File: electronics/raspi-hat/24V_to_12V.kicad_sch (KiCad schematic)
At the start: 11 parts

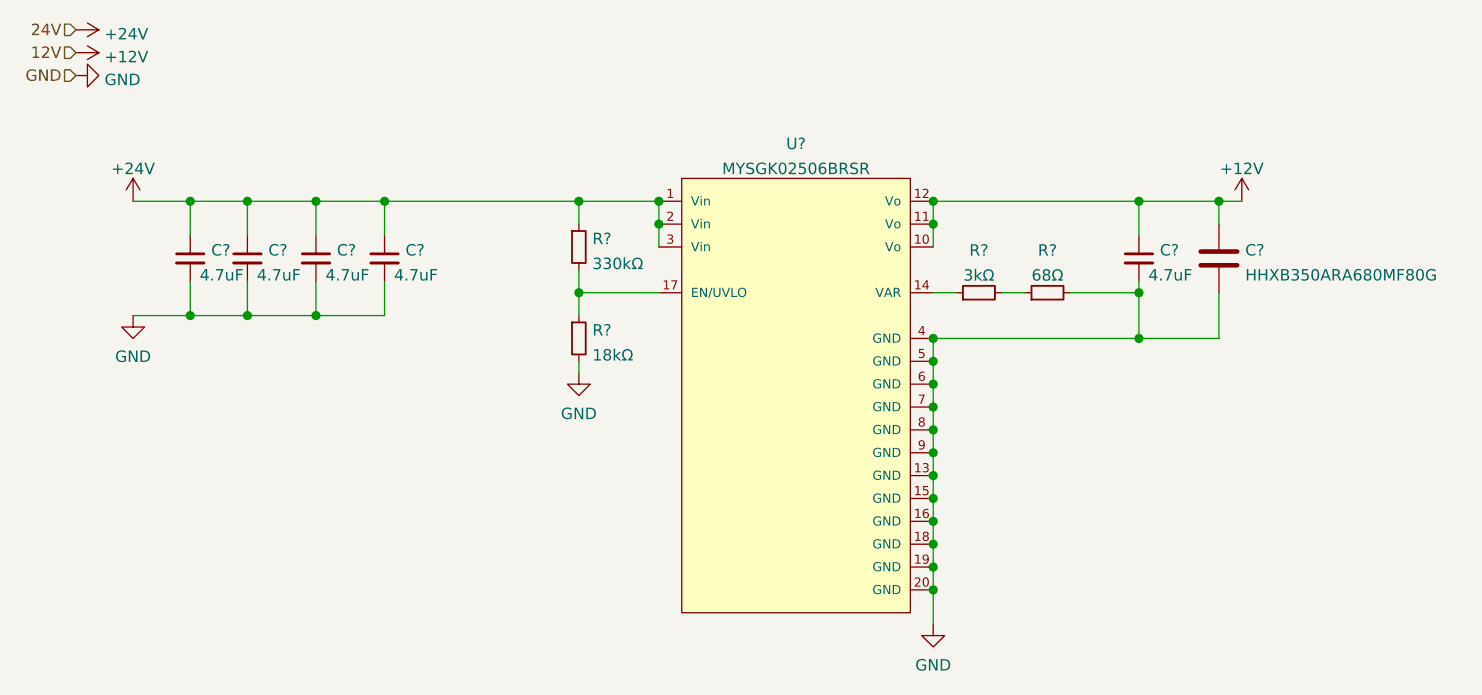
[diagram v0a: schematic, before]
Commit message: Finish adding MYMGA5R04RELA5RA
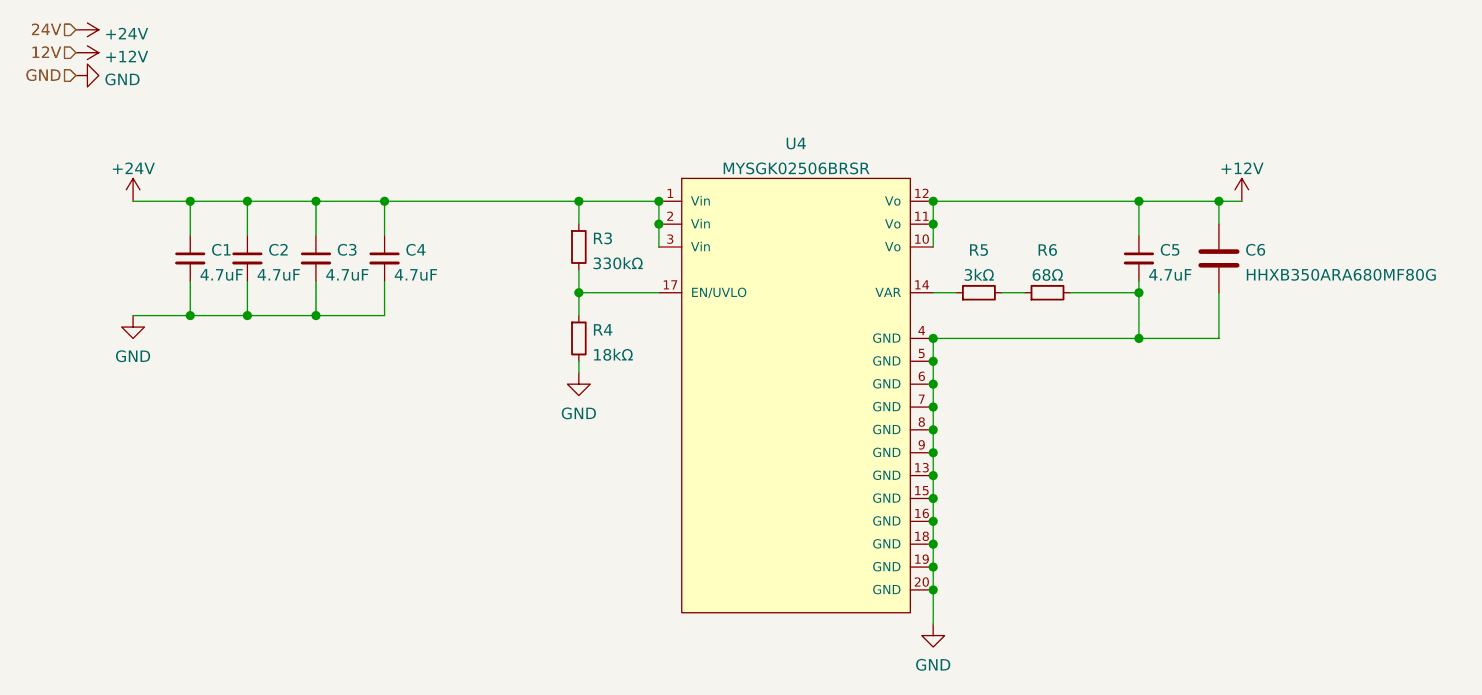
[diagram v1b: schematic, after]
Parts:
- gave numbers to parts that had none: 11
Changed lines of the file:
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@@
   (symbol (lib_id "power:+24V") (at 22.86 20.32 270) (unit 1)
     (in_bom yes) (on_board yes) (fields_autoplaced)
-    (property "Reference" "#PWR?" (id 0) (at 19.05 20.32 0)
+    (property "Reference" "#PWR0111" (id 0) (at 19.05 20.32 0)
       (effects (font (size 1.27 1.27)) hide)
     )
@@
   (symbol (lib_id "power:+12V") (at 22.86 22.86 270) (unit 1)
     (in_bom yes) (on_board yes) (fields_autoplaced)
-    (property "Reference" "#PWR?" (id 0) (at 19.05 22.86 0)
+    (property "Reference" "#PWR0112" (id 0) (at 19.05 22.86 0)
       (effects (font (size 1.27 1.27)) hide)
     )
@@
   (symbol (lib_id "power:+24V") (at 29.21 39.37 0) (unit 1)
     (in_bom yes) (on_board yes) (fields_autoplaced)
-    (property "Reference" "#PWR?" (id 0) (at 29.21 43.18 0)
+    (property "Reference" "#PWR0110" (id 0) (at 29.21 43.18 0)
       (effects (font (size 1.27 1.27)) hide)
     )
@@
   (symbol (lib_id "power:+12V") (at 152.4 39.37 0) (unit 1)
     (in_bom yes) (on_board yes) (fields_autoplaced)
-    (property "Reference" "#PWR?" (id 0) (at 152.4 43.18 0)
+    (property "Reference" "#PWR0108" (id 0) (at 152.4 43.18 0)
       (effects (font (size 1.27 1.27)) hide)
     )
@@
   (symbol (lib_id "power:GND") (at 22.86 25.4 90) (unit 1)
     (in_bom yes) (on_board yes) (fields_autoplaced)
-    (property "Reference" "#PWR?" (id 0) (at 29.21 25.4 0)
+    (property "Reference" "#PWR0113" (id 0) (at 29.21 25.4 0)
       (effects (font (size 1.27 1.27)) hide)
     )
@@
   (symbol (lib_id "power:GND") (at 29.21 52.07 0) (unit 1)
     (in_bom yes) (on_board yes) (fields_autoplaced)
-    (property "Reference" "#PWR?" (id 0) (at 29.21 58.42 0)
+    (property "Reference" "#PWR0109" (id 0) (at 29.21 58.42 0)
       (effects (font (size 1.27 1.27)) hide)
     )
@@
   (symbol (lib_id "power:GND") (at 78.74 58.42 0) (unit 1)
     (in_bom yes) (on_board yes) (fields_autoplaced)
-    (property "Reference" "#PWR?" (id 0) (at 78.74 64.77 0)
+    (property "Reference" "#PWR0114" (id 0) (at 78.74 64.77 0)
       (effects (font (size 1.27 1.27)) hide)
     )
@@
   (symbol (lib_id "power:GND") (at 118.11 86.36 0) (unit 1)
     (in_bom yes) (on_board yes) (fields_autoplaced)
-    (property "Reference" "#PWR?" (id 0) (at 118.11 92.71 0)
+    (property "Reference" "#PWR0107" (id 0) (at 118.11 92.71 0)
       (effects (font (size 1.27 1.27)) hide)
     )
@@
   (symbol (lib_id "Device:R_Small") (at 78.74 44.45 0) (unit 1)
     (in_bom yes) (on_board yes) (fields_autoplaced)
-    (property "Reference" "R?" (id 0) (at 80.2387 43.5415 0)
+    (property "Reference" "R3" (id 0) (at 80.2387 43.5415 0)
       (effects (font (size 1.27 1.27)) (justify left))
     )
@@
   (symbol (lib_id "Device:R_Small") (at 78.74 54.61 0) (unit 1)
     (in_bom yes) (on_board yes) (fields_autoplaced)
-    (property "Reference" "R?" (id 0) (at 80.2387 53.7015 0)
+    (property "Reference" "R4" (id 0) (at 80.2387 53.7015 0)
       (effects (font (size 1.27 1.27)) (justify left))
     )
@@
   (symbol (lib_id "Device:R_Small") (at 123.19 49.53 90) (unit 1)
     (in_bom yes) (on_board yes) (fields_autoplaced)
-    (property "Reference" "R?" (id 0) (at 123.19 44.8268 90))
+    (property "Reference" "R5" (id 0) (at 123.19 44.8268 90))
     (property "Value" "3kΩ" (id 1) (at 123.19 47.6019 90))
     (property "Footprint" "" (id 2) (at 123.19 49.53 0)
@@
   (symbol (lib_id "Device:R_Small") (at 130.81 49.53 90) (unit 1)
     (in_bom yes) (on_board yes) (fields_autoplaced)
-    (property "Reference" "R?" (id 0) (at 130.81 44.8268 90))
+    (property "Reference" "R6" (id 0) (at 130.81 44.8268 90))
     (property "Value" "68Ω" (id 1) (at 130.81 47.6019 90))
     (property "Footprint" "" (id 2) (at 130.81 49.53 0)
@@
   (symbol (lib_id "Device:C_Small") (at 35.56 45.72 0) (unit 1)
     (in_bom yes) (on_board yes)
-    (property "Reference" "C?" (id 0) (at 37.8842 44.8115 0)
+    (property "Reference" "C1" (id 0) (at 37.8842 44.8115 0)
       (effects (font (size 1.27 1.27)) (justify left))
     )
@@
   (symbol (lib_id "Device:C_Small") (at 41.91 45.72 0) (unit 1)
     (in_bom yes) (on_board yes)
-    (property "Reference" "C?" (id 0) (at 44.2342 44.8115 0)
+    (property "Reference" "C2" (id 0) (at 44.2342 44.8115 0)
       (effects (font (size 1.27 1.27)) (justify left))
     )
@@
   (symbol (lib_id "Device:C_Small") (at 49.53 45.72 0) (unit 1)
     (in_bom yes) (on_board yes)
-    (property "Reference" "C?" (id 0) (at 51.8542 44.8115 0)
+    (property "Reference" "C3" (id 0) (at 51.8542 44.8115 0)
       (effects (font (size 1.27 1.27)) (justify left))
     )
@@
   (symbol (lib_id "Device:C_Small") (at 57.15 45.72 0) (unit 1)
     (in_bom yes) (on_board yes)
-    (property "Reference" "C?" (id 0) (at 59.4742 44.8115 0)
+    (property "Reference" "C4" (id 0) (at 59.4742 44.8115 0)
       (effects (font (size 1.27 1.27)) (justify left))
     )
@@
   (symbol (lib_id "Device:C_Small") (at 140.97 45.72 0) (unit 1)
     (in_bom yes) (on_board yes)
-    (property "Reference" "C?" (id 0) (at 143.2942 44.8115 0)
+    (property "Reference" "C5" (id 0) (at 143.2942 44.8115 0)
       (effects (font (size 1.27 1.27)) (justify left))
     )
@@
   (symbol (lib_id "Device:C") (at 149.86 45.72 0) (unit 1)
     (in_bom yes) (on_board yes) (fields_autoplaced)
-    (property "Reference" "C?" (id 0) (at 152.7811 44.8115 0)
+    (property "Reference" "C6" (id 0) (at 152.7811 44.8115 0)
       (effects (font (size 1.27 1.27)) (justify left))
     )
@@
   (symbol (lib_id "MYSGK02506BRSR:MYSGK02506BRSR") (at 85.09 39.37 0) (unit 1)
     (in_bom yes) (on_board yes) (fields_autoplaced)
-    (property "Reference" "U?" (id 0) (at 102.87 32.9904 0))
+    (property "Reference" "U4" (id 0) (at 102.87 32.9904 0))
     (property "Value" "MYSGK02506BRSR" (id 1) (at 102.87 35.7655 0))
     (property "Footprint" "Murata-MYSGK-06-0-0-*" (id 2) (at 85.09 29.21 0)

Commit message: Start laying out PCB for raspberry pi hat
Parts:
- C1, C2, C3, C4, C5: footprint (none) -> Capacitor_SMD:C_0603_1608Metric
- R3, R4, R5, R6: footprint (none) -> Resistor_SMD:R_0603_1608Metric
- U4: footprint Murata-MYSGK-06-0-0-* -> MYSGK02506BRSR:Murata-MYSGK-06-0-0-MFG
